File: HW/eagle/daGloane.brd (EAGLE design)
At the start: 100 x 80 mm, 84 parts, among them IC1 MCP1252-33X50, U1 STM32F10XTXU6, X2 USB_MICROB_PLUG_MT

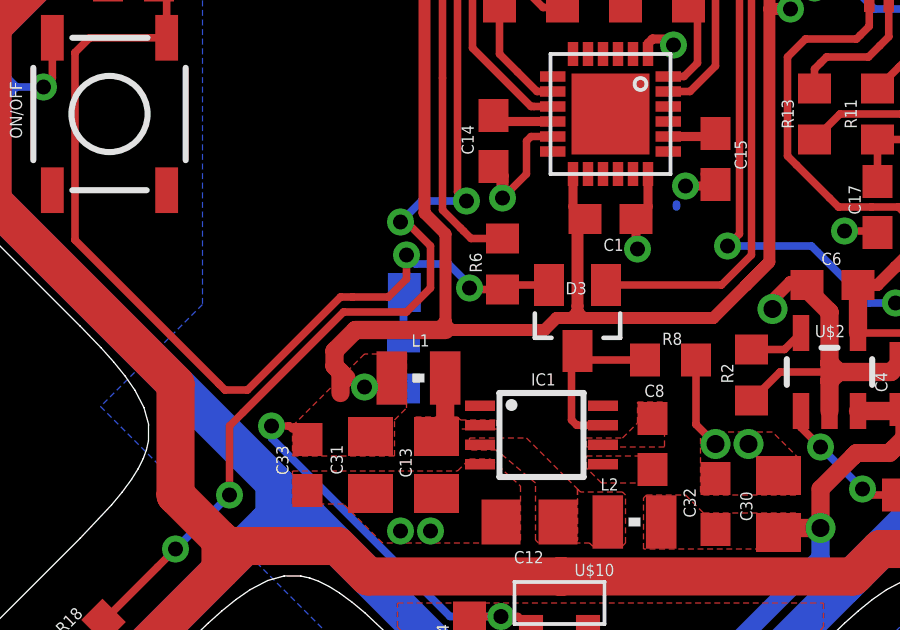
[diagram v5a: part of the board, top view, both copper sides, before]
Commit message: changed connection of the bluetooth module's AT pin.
It is now connected to the pwr_on/off logic. This will set it into AT mode at startup so the µC can configure the module. Once the configuration is done the µC can set it into operating mode by simply sending a AT+RESET command.
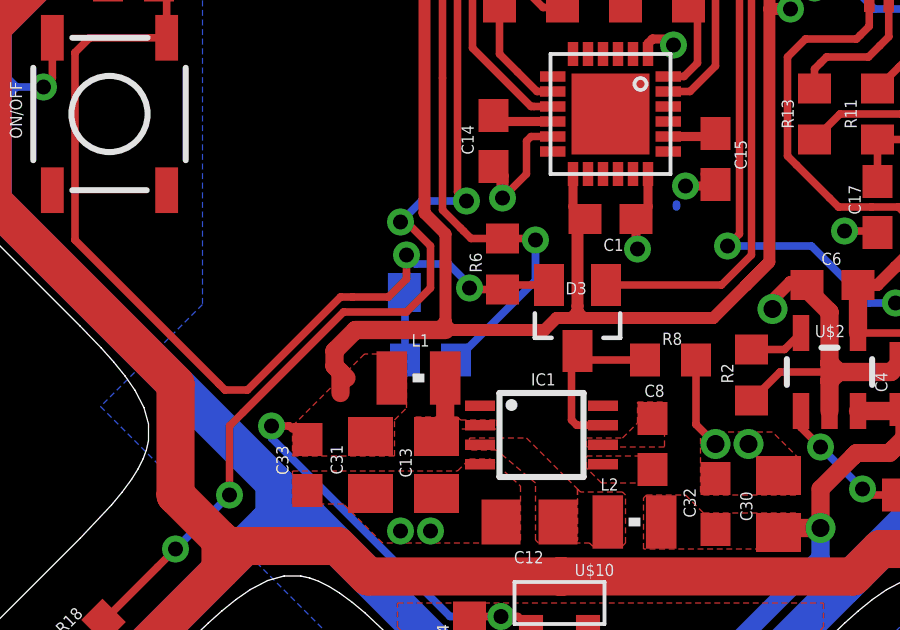
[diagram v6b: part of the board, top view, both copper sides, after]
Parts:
- moved R30 0.91 mm to (34.5, 32.3), turned to 180 degrees
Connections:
- net PWR_OFF: now also R30.2
- net VCC: no longer R30.2
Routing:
- net PWR_OFF: track 18.1 -> 24.3 mm, vias 0 -> 1
- net VCC: track 133.4 -> 132.1 mm, vias 6 -> 5
- net N$26: track 1.51 -> 2.31 mm
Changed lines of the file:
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@@
 <?xml version="1.0" encoding="utf-8"?>
 <!DOCTYPE eagle SYSTEM "eagle.dtd">
-<eagle version="6.2">
+<eagle version="6.1">
 <drawing>
 <settings>
@@
 </element>
 <element name="U$5" library="daGloane" package="BLUETOOTH_REDUCED" value="BLUETOOTH_REDUCED" x="40.5" y="40.6" rot="MR270"/>
-<element name="R30" library="rcl" package="R0603" value="1k" x="33.6" y="32.2" smashed="yes" rot="MR270">
-<attribute name="NAME" x="33.011" y="32.889" size="0.4064" layer="26" font="vector" rot="MR270"/>
-<attribute name="VALUE" x="35.632" y="33.089" size="1.27" layer="28" rot="MR270"/>
+<element name="R30" library="rcl" package="R0603" value="1k" x="34.5" y="32.3" smashed="yes" rot="MR180">
+<attribute name="NAME" x="33.811" y="31.711" size="0.4064" layer="26" font="vector" rot="MR180"/>
+<attribute name="VALUE" x="33.611" y="34.332" size="1.27" layer="28" rot="MR180"/>
 </element>
 <element name="U$6" library="daGloane" package="3A_BLDC_CONTROLLER" value="3A_BLDC_CONTROLLER" x="12.5" y="12.5" rot="R315"/>
@@
 <wire x1="36.8478875" y1="23.75" x2="37.415" y2="23.75" width="0.254" layer="1"/>
 <wire x1="37.415" y1="23.75" x2="37.85" y2="23.315" width="0.254" layer="1"/>
-<contactref element="R30" pad="2"/>
 <via x="29.2" y="30.1" extent="1-16" drill="0.5"/>
 <via x="36.8478875" y="23.75" extent="1-16" drill="0.5"/>
@@
 <vertex x="29.9" y="30.1"/>
 </polygon>
-<wire x1="33.6" y1="31.35" x2="32.35" y2="31.35" width="0.254" layer="16"/>
-<wire x1="32.35" y1="31.35" x2="32.3" y2="31.4" width="0.254" layer="16"/>
-<via x="32.3" y="31.4" extent="1-16" drill="0.5"/>
 <wire x1="29.2" y1="30.1" x2="29.8" y2="30.1" width="0.254" layer="1"/>
 <wire x1="29.8" y1="30.1" x2="29.9" y2="30" width="0.254" layer="1"/>
@@
 <wire x1="35.3" y1="49.1" x2="34.9" y2="48.7" width="0.254" layer="1"/>
 <wire x1="34.9" y1="48.7" x2="34.9" y2="47.9" width="0.254" layer="1"/>
+<contactref element="R30" pad="2"/>
+<via x="38" y="36.3" extent="1-16" drill="0.5"/>
+<wire x1="38" y1="36.3" x2="37.95" y2="36.35" width="0.254" layer="1"/>
+<wire x1="37.95" y1="36.35" x2="36.9" y2="36.35" width="0.254" layer="1"/>
+<wire x1="35.35" y1="32.3" x2="38" y2="34.95" width="0.254" layer="16"/>
+<wire x1="38" y1="34.95" x2="38" y2="36.3" width="0.254" layer="16"/>
 </signal>
 <signal name="N$23">
@@
 <contactref element="R30" pad="1"/>
 <wire x1="33.63" y1="34.55" x2="33.6" y2="34.52" width="0.254" layer="16"/>
-<wire x1="33.6" y1="34.52" x2="33.6" y2="33.05" width="0.254" layer="16"/>
+<wire x1="33.6" y1="34.52" x2="33.65" y2="34.52" width="0.254" layer="16"/>
+<wire x1="33.65" y1="34.52" x2="33.65" y2="32.3" width="0.254" layer="16"/>
 </signal>
 <signal name="MT_PAD2">

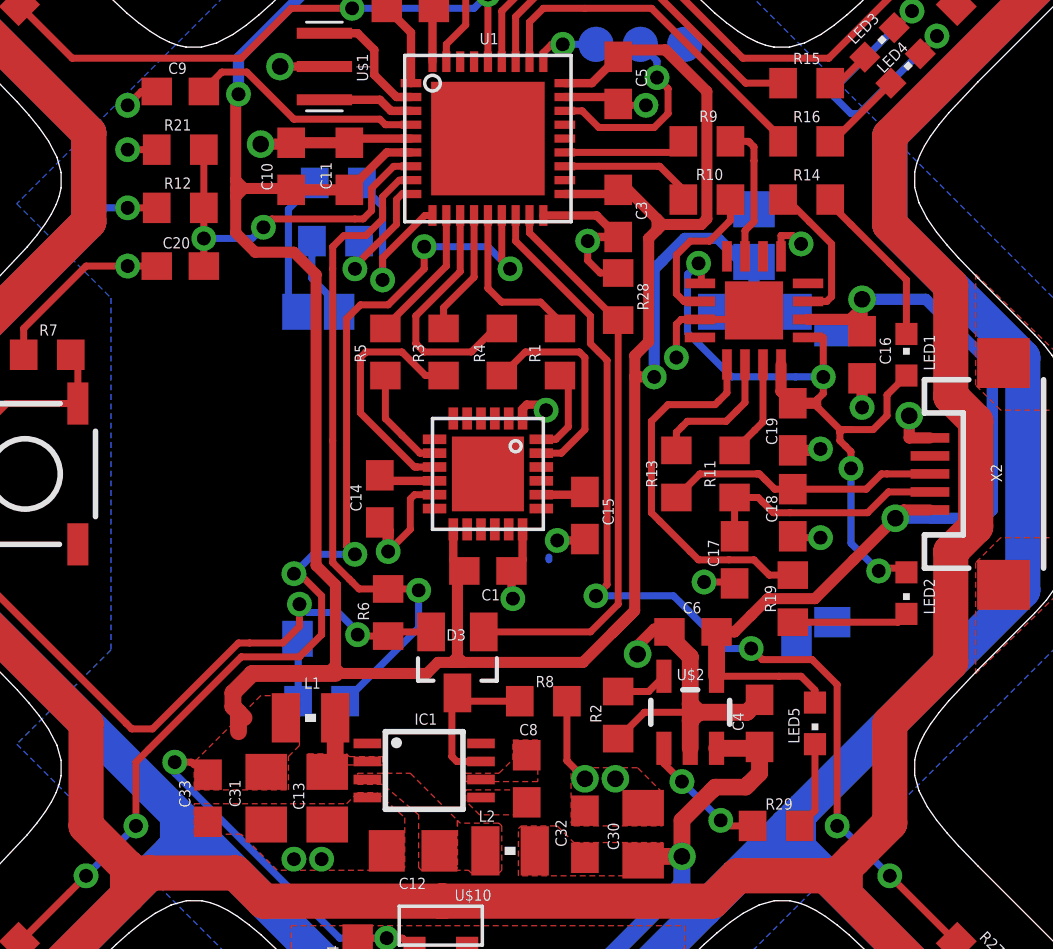
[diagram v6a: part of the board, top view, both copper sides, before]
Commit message: bluetooth module replaced with new version
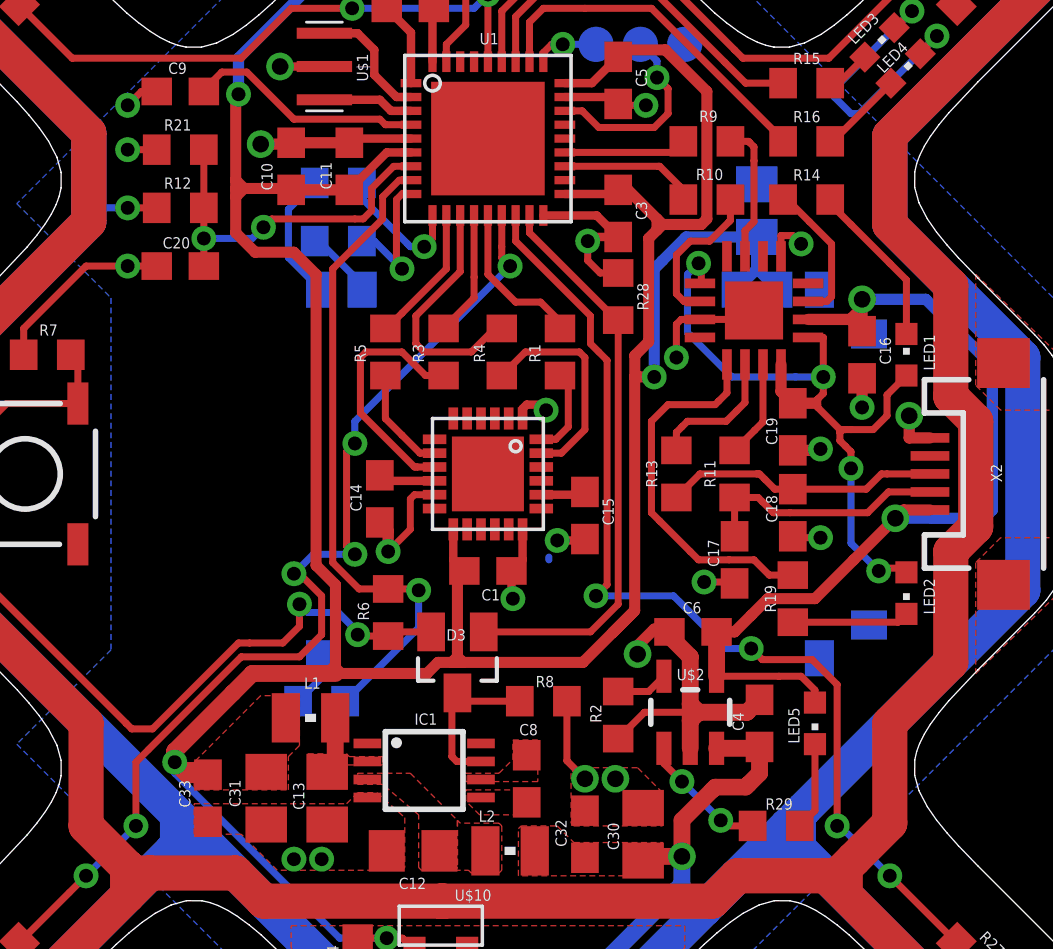
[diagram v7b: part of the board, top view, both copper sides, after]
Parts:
- moved C21 0.91 mm to (50.2, 50.0)
- moved R23 0.10 mm to (35.1, 48.9)
- moved U$5 0.10 mm to (40.5, 40.5)
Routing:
- net VCC: track 132.1 -> 136.2 mm
- net MOT1: track 40.5 -> 37.0 mm
- net USART2_RX: track 7.04 -> 4.77 mm
- net N$7: track 5.36 -> 4.72 mm

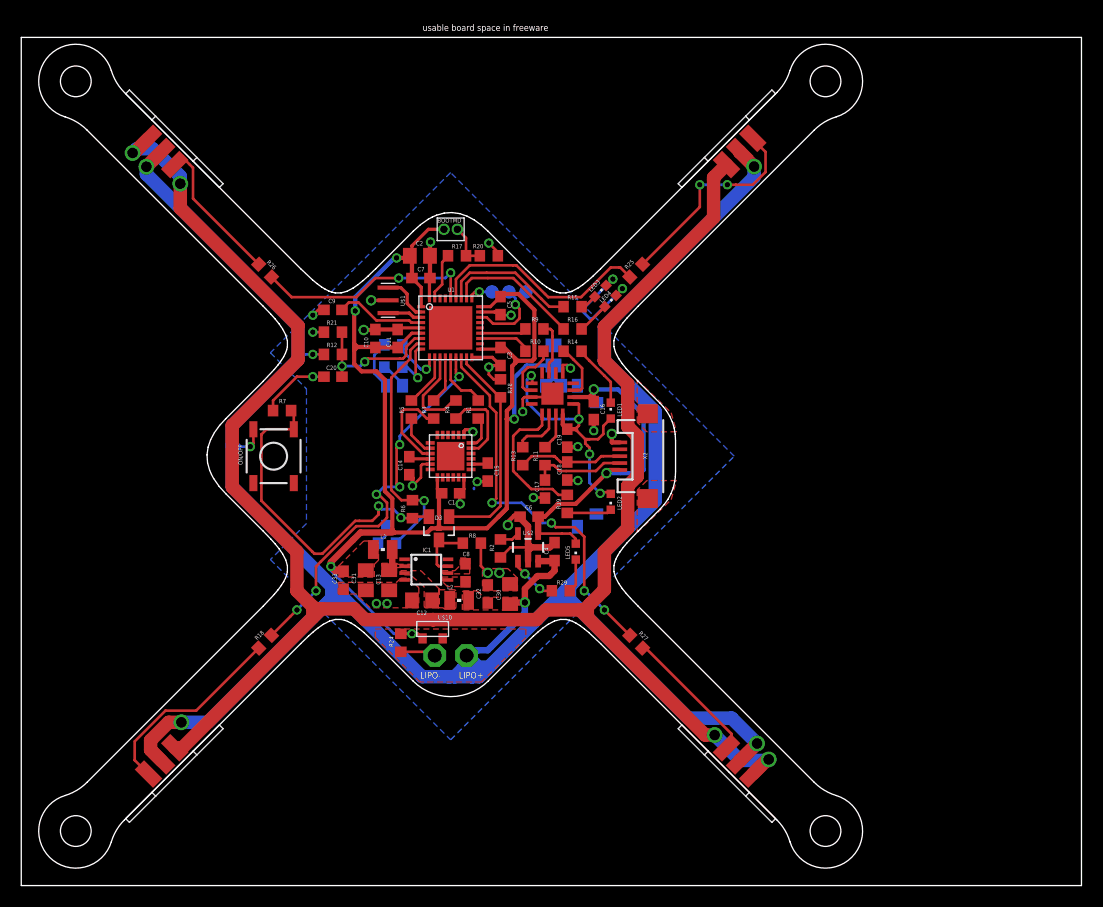
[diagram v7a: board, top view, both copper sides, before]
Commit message: stm32 vqfpn36 package cream layer divided in 4 segments
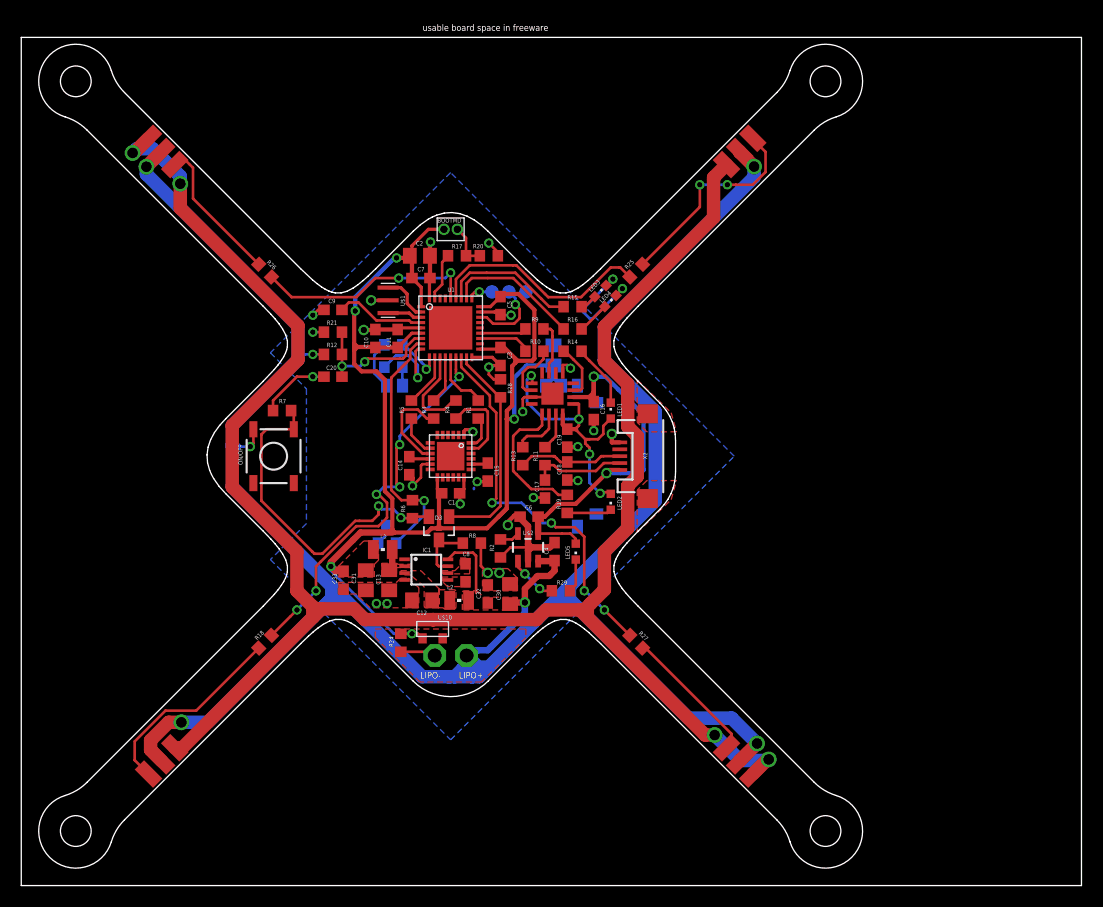
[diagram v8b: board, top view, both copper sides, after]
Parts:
- C4: value 1µF -> 4.7
- C6: value 1µF -> 4.7µF
- turned R23 to 180 degrees
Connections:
- net LIPO: now also IC1.8
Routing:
- net LIPO: track 226.1 -> 232.6 mm
- net USART2_TX: track 5.20 -> 8.37 mm
- net VBUS: track 34.1 -> 37.0 mm
- net N$15: track 2.55 -> 1.75 mm
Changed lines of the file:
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@@
 <attribute name="VALUE" x="46.8475" y="31.7095" size="0.4064" layer="27"/>
 </element>
-<element name="C6" library="rcl" package="C0603" value="1µF" x="47.9" y="34.8" smashed="yes">
+<element name="C6" library="rcl" package="C0603" value="4.7µF" x="47.9" y="34.8" smashed="yes">
 <attribute name="NAME" x="47.53" y="35.47" size="0.4064" layer="25"/>
 <attribute name="VALUE" x="46.63" y="32.26" size="0.4064" layer="27"/>
 </element>
-<element name="C4" library="rcl" package="C0603" value="1µF" x="50.3" y="31.5" smashed="yes" rot="R90">
+<element name="C4" library="rcl" package="C0603" value="4.7" x="50.3" y="31.5" smashed="yes" rot="R90">
 <attribute name="NAME" x="49.73" y="31.23" size="0.4064" layer="25" rot="R90"/>
 <attribute name="VALUE" x="52.84" y="30.23" size="0.4064" layer="27" rot="R90"/>
@@
 <attribute name="VALUE" x="35.989" y="48.967996875" size="0.4064" layer="28" rot="MR0"/>
 </element>
-<element name="R23" library="rcl" package="R0603" value="1k" x="35.1" y="48.9" smashed="yes" rot="MR0">
-<attribute name="NAME" x="35.689" y="49.588996875" size="0.4064" layer="26" rot="MR0"/>
-<attribute name="VALUE" x="35.989" y="46.867996875" size="0.4064" layer="28" rot="MR0"/>
+<element name="R23" library="rcl" package="R0603" value="1k" x="35.1" y="48.9" smashed="yes" rot="MR180">
+<attribute name="NAME" x="34.511" y="48.211003125" size="0.4064" layer="26" rot="MR180"/>
+<attribute name="VALUE" x="34.211" y="50.932003125" size="0.4064" layer="28" rot="MR180"/>
 </element>
 <element name="D3" library="diode" package="SOT23" value="BAT54C" x="39.4" y="33.7" smashed="yes" rot="R180">
@@
 <wire x1="26.7" y1="50.1" x2="26.15" y2="49.55" width="0.254" layer="16"/>
 <wire x1="26.15" y1="49.55" x2="26.05" y2="49.55" width="0.254" layer="16"/>
+<contactref element="IC1" pad="8"/>
+<wire x1="40.25" y1="30.775" x2="40.875" y2="31.4" width="0.254" layer="1"/>
+<wire x1="40.875" y1="31.4" x2="42.6" y2="31.4" width="0.254" layer="1"/>
+<wire x1="42.6" y1="31.4" x2="42.9" y2="31.1" width="0.254" layer="1"/>
+<wire x1="42.9" y1="31.1" x2="42.9" y2="27.6" width="0.254" layer="1"/>
 </signal>
 <signal name="VOLTAGE">
@@
 <wire x1="52.05" y1="46.075" x2="53.575" y2="46.075" width="0.4064" layer="1"/>
 <wire x1="54" y1="45.65" x2="53.575" y2="46.075" width="0.4064" layer="1"/>
-<via x="54" y="46.8" extent="1-16" drill="0.6"/>
+<via x="54" y="48" extent="1-16" drill="0.6"/>
 <wire x1="57.5" y1="45.6" x2="58.7" y2="44.4" width="0.4064" layer="16"/>
 <wire x1="58.7" y1="44.4" x2="58.7" y2="39.2" width="0.4064" layer="16"/>
@@
 <via x="55.2" y="38.9" extent="1-16" drill="0.6"/>
 <wire x1="57.5" y1="45.6" x2="56.3" y2="46.8" width="0.4064" layer="16"/>
-<wire x1="56.3" y1="46.8" x2="54" y2="46.8" width="0.4064" layer="16"/>
-<wire x1="54" y1="46.8" x2="54" y2="45.65" width="0.4064" layer="1"/>
+<wire x1="54" y1="48" x2="54" y2="45.65" width="0.4064" layer="1"/>
 <wire x1="53.575" y1="46.075" x2="54" y2="46.5" width="0.4064" layer="1"/>
-<wire x1="54" y1="46.5" x2="54" y2="46.8" width="0.4064" layer="1"/>
+<wire x1="54" y1="46.5" x2="54" y2="48" width="0.4064" layer="1"/>
 <wire x1="50" y1="35.4" x2="50.6" y2="36" width="0.4" layer="1"/>
 <wire x1="50.6" y1="36" x2="52.3" y2="36" width="0.4" layer="1"/>
@@
 <wire x1="55.5" y1="39.2" x2="55.2" y2="38.9" width="0.4" layer="1"/>
 <wire x1="50" y1="35.4" x2="49.4" y2="34.8" width="0.4" layer="1"/>
-<wire x1="49.4" y1="34.8" x2="48.75" y2="34.8" width="0.4" layer="1"/>
 <wire x1="48.75" y1="34.8" x2="48.7" y2="34.8" width="0.4" layer="1"/>
 <wire x1="48.75" y1="34.8" x2="48.7" y2="34.8" width="0.4" layer="1"/>
@@
 <wire x1="51" y1="33.2" x2="48.7501" y2="33.2" width="0.254" layer="1"/>
 <wire x1="48.7501" y1="33.2" x2="48.75" y2="33.2001" width="0.254" layer="1"/>
+<wire x1="54" y1="48" x2="55.1" y2="48" width="0.4064" layer="16"/>
+<wire x1="55.1" y1="48" x2="56.3" y2="46.8" width="0.4064" layer="16"/>
+<wire x1="49.4" y1="34.8" x2="48.75" y2="34.8" width="0.4" layer="1"/>
 </signal>
 <signal name="N$5">
@@
 <wire x1="38.5" y1="49.825" x2="38.5" y2="49" width="0.254" layer="1"/>
 <wire x1="38.5" y1="49" x2="38.2" y2="48.7" width="0.254" layer="1"/>
-<wire x1="35.95" y1="50.9" x2="35.95" y2="50.45" width="0.254" layer="16"/>
-<wire x1="35.95" y1="50.45" x2="37.6" y2="48.8" width="0.254" layer="16"/>
-<wire x1="37.6" y1="48.8" x2="37.7" y2="48.7" width="0.254" layer="16"/>
-<wire x1="37.7" y1="48.7" x2="38.2" y2="48.7" width="0.254" layer="16"/>
+<wire x1="35.95" y1="50.9" x2="36.2" y2="50.9" width="0.254" layer="16"/>
+<wire x1="36.2" y1="50.9" x2="37.8" y2="49.3" width="0.254" layer="16"/>
+<wire x1="37.8" y1="49.3" x2="38.2" y2="48.9" width="0.254" layer="16"/>
+<wire x1="38.2" y1="48.9" x2="38.2" y2="48.7" width="0.254" layer="16"/>
 </signal>
 <signal name="USART2_TX">
@@
 <wire x1="37.2" y1="50.4" x2="37.2" y2="49.5" width="0.25" layer="1"/>
 <via x="37.4" y="47.9" extent="1-16" drill="0.5"/>
-<wire x1="35.85" y1="48.8" x2="35.95" y2="48.9" width="0.254" layer="16"/>
 <wire x1="37.4" y1="47.9" x2="37.2" y2="48.1" width="0.254" layer="1"/>
 <wire x1="37.2" y1="48.1" x2="37.2" y2="49.5" width="0.254" layer="1"/>
-<wire x1="35.95" y1="48.9" x2="36.4" y2="48.9" width="0.254" layer="16"/>
-<wire x1="36.4" y1="48.9" x2="37.4" y2="47.9" width="0.254" layer="16"/>
+<wire x1="37.4" y1="47.9" x2="37.4" y2="49.1" width="0.254" layer="16"/>
+<wire x1="34.25" y1="48.9" x2="35.35" y2="50" width="0.254" layer="16"/>
+<wire x1="35.35" y1="50" x2="35.6" y2="50" width="0.254" layer="16"/>
+<wire x1="35.6" y1="50" x2="36.5" y2="50" width="0.254" layer="16"/>
+<wire x1="36.5" y1="50" x2="37.4" y2="49.1" width="0.254" layer="16"/>
 </signal>
 <signal name="MOT4">
@@
 <contactref element="U$5" pad="P$2"/>
 <wire x1="35.96" y1="47.15" x2="35.96" y2="47.34" width="0.254" layer="16"/>
-<wire x1="35.96" y1="47.34" x2="35.2" y2="48.1" width="0.254" layer="16"/>
-<wire x1="35.2" y1="48.1" x2="34.4" y2="48.9" width="0.254" layer="16"/>
-<wire x1="34.4" y1="48.9" x2="34.25" y2="48.9" width="0.254" layer="16"/>
+<wire x1="35.96" y1="47.34" x2="35.95" y2="47.35" width="0.254" layer="16"/>
+<wire x1="35.95" y1="47.35" x2="35.95" y2="48.9" width="0.254" layer="16"/>
 </signal>
 <signal name="PWR_ON_µC">
